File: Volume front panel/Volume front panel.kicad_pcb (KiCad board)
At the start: 2 copper layers, 210.2 x 50.9 mm, 44 parts, among them IC1 MC7805BD2TR4G, IC2 TLC5947DAPR, IC3 MC7805BD2TR4G, J1 26-60-4023, J2 26-60-4023, J3 4328, U1 PEC11R-4330F-S0012, U2 TSOP39238, U3 ISO1541

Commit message: seperated front panel board
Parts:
- moved J2 228.6 mm to (283.5, 78.9), turned to 180 degrees
- moved C13 222.6 mm to (275.0, 79.0), turned to -90 degrees
- moved IC3 214.0 mm to (278.5, 67.0), turned to 0 degrees
- moved C14 205.4 mm to (266.5, 64.0), turned to 180 degrees
- moved C17 202.2 mm to (266.5, 67.0), turned to 180 degrees
- moved C16 199.1 mm to (266.5, 70.0), turned to 180 degrees
- moved J3 189.5 mm to (265.0, 80.0), turned to -90 degrees
- moved R10 186.6 mm to (260.0, 83.0), turned to -90 degrees
- moved R9 183.3 mm to (260.0, 78.0)
- moved U3 170.2 mm to (254.0, 80.0), turned to 0 degrees
- moved C4 14.7 mm to (218.5, 60.5), turned to 180 degrees
- moved J1 13.5 mm to (242.0, 77.1)
- moved C3 12.0 mm to (229.0, 77.0)
- moved C10 11.0 mm to (218.5, 64.0), turned to 180 degrees
- moved IC1 10.5 mm to (230.0, 64.0), turned to 0 degrees
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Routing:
- net Net-(U3-SCL2): track 0.00 -> 7.55 mm
- net Net-(C13-+): track 20.3 -> 27.3 mm
- net Net-(U3-SDA2): track 0.00 -> 6.81 mm
- net GNDI: vias 0 -> 52
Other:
- board size 210.2 x 50.9 mm -> 208 x 50.9 mm

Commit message: moving everything onto front panel, switching psu, no iso
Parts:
- removed the C10 at (218.5, 64.0)
- removed the C11 at (218.5, 67.5)
- removed C13: UUD1V101MNL1GS, Samacsys:CAPAE830X1050N
- removed C14: .1uf, Capacitor_SMD:C_1206_3216Metric
- removed C16: 10uf, Capacitor_SMD:C_1206_3216Metric
- removed C17: 1uf, Capacitor_SMD:C_1206_3216Metric
- removed the C3 at (229.0, 77.0)
- removed the C4 at (218.5, 60.5)
- removed the H1 at (45.0, 50.0)
- removed the H2 at (45.0, 90.0)
- removed the IC1 at (230.0, 64.0)
- removed IC3: MC7805BD2TR4G, Samacsys:TO254P1420X457-4N
- removed J3: 4328, Snapeda_8:ADAFRUIT_4328
- removed R10, R9: 1k, Resistor_SMD:R_1206_3216Metric
- removed the R5 at (190.5, 82.5)
- removed the R6 at (193.0, 82.5)
- removed U3: ISO1541, Package_SO:SOIC-8_3.9x4.9mm_P1.27mm
- added C12: 0.1uf, Capacitor_SMD:C_1206_3216Metric, F.Cu at (159.5, 59.0)
- added C7: UUD1V101MNL1GS, Samacsys:CAPAE830X1050N, F.Cu at (190.0, 55.0)
- added C9: UUD1V101MNL1GS, Samacsys:CAPAE830X1050N, F.Cu at (190.0, 79.0)
- added IC2: TPIC6B595DWR, Samacsys:SOIC127P1030X265-20N, F.Cu at (151.5, 53.0)
- added L1: 150uh, Inductor_SMD:L_Bourns_SRR1260, F.Cu at (190.0, 67.0)
- added PS2: TMPW_5-105, Samacsys:TMPW5112, F.Cu at (202.5, 80.4)
- added R7: 10k, Resistor_SMD:R_1206_3216Metric, F.Cu at (160.5, 49.0)
- J2: value 26-60-4023 -> 10129381-908001BLF; footprint Samacsys:26604023 -> Samacsys:10129381908001BLF
- U1: moved to B.Cu
- moved J2 119.6 mm to (165.8, 57.8), turned to 90 degrees
- moved C1 56.6 mm to (162.0, 85.0), turned to 180 degrees
- moved H2 49.6 mm to (85.5, 87.0)
- moved H1 48.6 mm to (86.5, 47.0)
- moved U1 38.6 mm to (119.0, 74.0), turned to 0 degrees
- moved C3 33.6 mm to (119.5, 56.0)
- moved C4 33.6 mm to (121.9, 71.1)
- moved C5 33.6 mm to (124.5, 56.0)
- moved R1 33.6 mm to (114.5, 59.0)
- moved R2 33.6 mm to (118.5, 62.0)
- moved R3 33.6 mm to (124.5, 62.0)
- moved R4 33.6 mm to (128.5, 59.0)
- moved A1 31.6 mm to (176.6, 63.4)
- moved C2 31.6 mm to (170.5, 82.0)
- moved C10 29.0 mm to (77.1, 62.5)
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- renumbered C12 to C10, C15 to C11, C5 to C3, C6 to C4, C7 to C5, C8 to C6, C9 to C8, H3 to H1, H4 to H2, H5 to H3, H6 to H4, IC2 to IC1, R7 to R5, R8 to R6
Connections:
- A1 pad 10: unconnected-(A1-D7-Pad10) -> unmute
- A1 pad 11: unconnected-(A1-D8-Pad11) -> shift_reg_strobe
- A1 pad 12: unconnected-(A1-D9-Pad12) -> shift_reg_clock
- A1 pad 23: SDA -> unconnected-(A1-A4-Pad23)
- A1 pad 24: SCL -> unconnected-(A1-A5-Pad24)
- A1 pad 5: unconnected-(A1-D2-Pad5) -> Net-(A1-D2)
- A1 pad 9: Net-(A1-D6) -> r_data
- C3 pad 2: Net-(A1-D3) -> Net-(A1-D2)
- C4 pad 1: Net-(A1-D5) -> Net-(A1-D4)
- C5 pad 1: Net-(A1-D4) -> Net-(A1-D3)
- C8 pad 1: Net-(A1-D6) -> Net-(A1-D5)
- J1 pad 2: GNDD -> Net-(PS2-AC_IN_(L))
- J2 pad 1: Net-(C13-+) -> +5V
- J2 pad 2: GNDI -> +5V
- R1 pad 2: Net-(A1-D3) -> Net-(A1-D2)
- R4 pad 2: Net-(A1-D4) -> Net-(A1-D3)
- U1 pad 2: Net-(A1-D5) -> Net-(A1-D4)
- U2 pad 3: Net-(A1-D6) -> Net-(A1-D5)
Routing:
- net +5V-iso: track 44.3 -> 0.00 mm
- net Net-(C13-+): track 27.3 -> 0.00 mm
- net Net-(U3-SCL2): track 7.55 -> 0.00 mm
- net Net-(U3-SDA2): track 6.81 -> 0.00 mm
- net GNDI: vias 52 -> 0
- removed copper zone on B.Cu, net GNDI
- removed copper zone on F.Cu, net GNDI
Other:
- board size 208 x 50.9 mm -> 171 x 50.9 mm

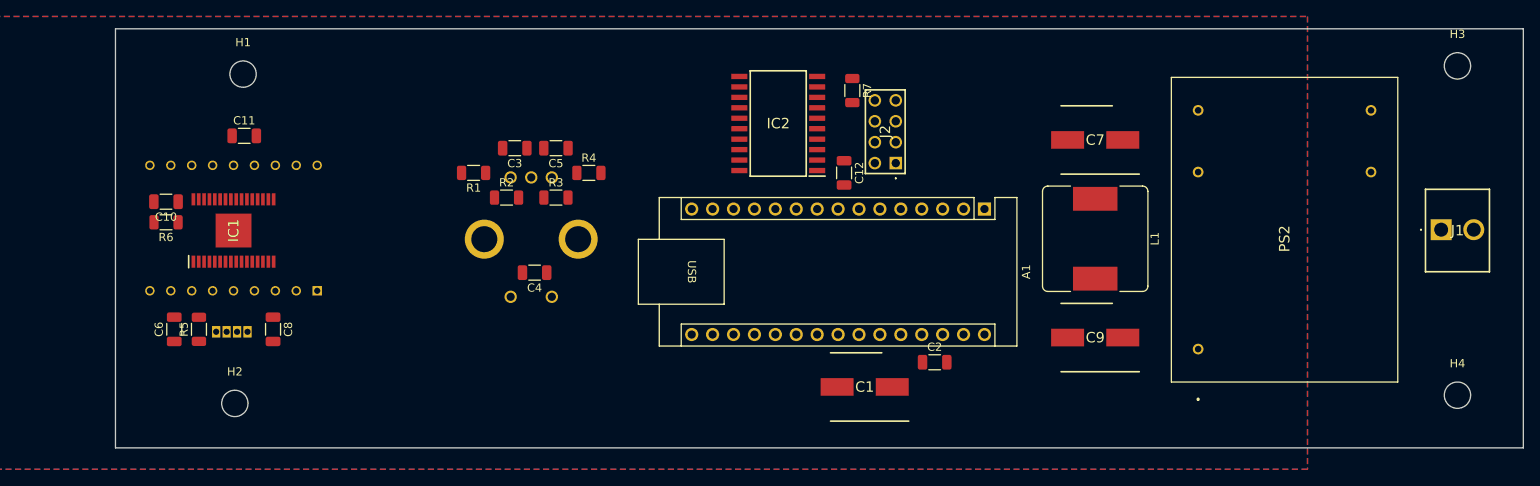
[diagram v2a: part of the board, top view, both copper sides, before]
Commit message: seperate psu, traco. All logic and such on front panel
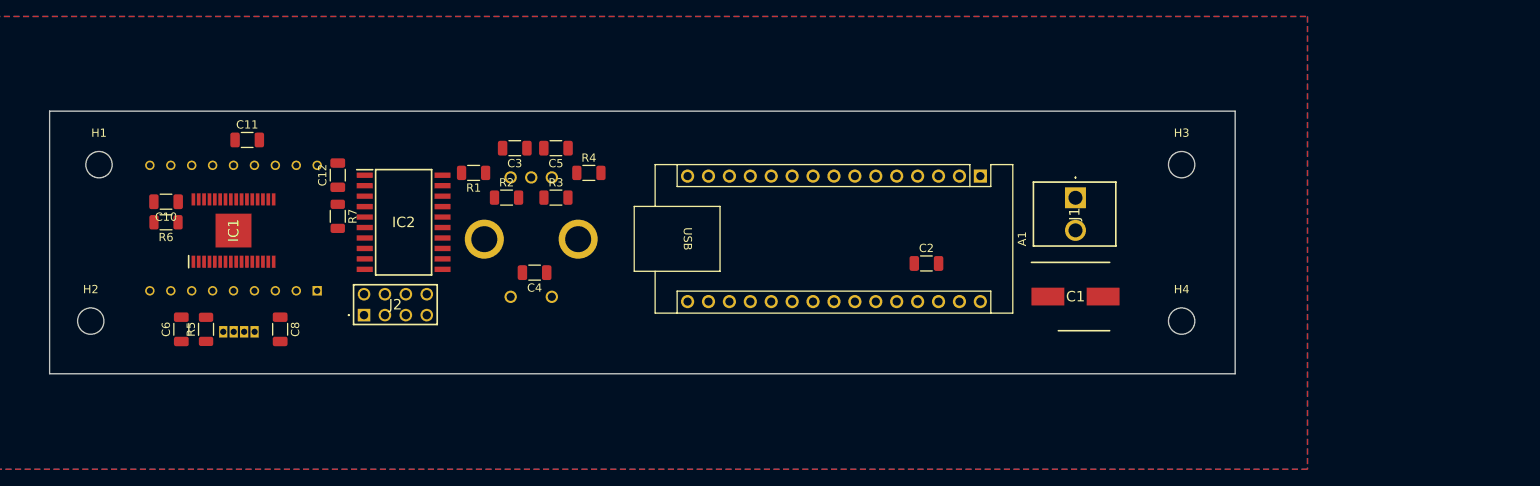
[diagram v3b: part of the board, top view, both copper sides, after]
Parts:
- removed C7, C9: UUD1V101MNL1GS, Samacsys:CAPAE830X1050N
- removed L1: 150uh, Inductor_SMD:L_Bourns_SRR1260
- removed PS2: TMPW_5-105, Samacsys:TMPW5112
- moved J2 67.2 mm to (101.2, 76.3), turned to 0 degrees
- moved R7 64.3 mm to (98.0, 64.3)
- moved C12 61.5 mm to (98.0, 59.3), turned to 90 degrees
- moved IC2 47.1 mm to (106.0, 65.0), turned to 0 degrees
- moved J1 44.6 mm to (187.6, 62.0), turned to 90 degrees
- moved H3 35.6 mm to (200.5, 58.0)
- moved H4 34.7 mm to (200.5, 77.0)
- moved C1 27.9 mm to (187.6, 74.0), turned to 0 degrees
- moved H1 20.7 mm to (69.0, 58.0)
- moved H2 20.2 mm to (68.0, 77.0)
- moved C2 12.0 mm to (169.5, 70.0)
- moved A1 4.03 mm to (176.1, 59.4)
- moved C6 0.86 mm to (79.0, 78.0)
- moved C8 0.86 mm to (91.0, 78.0)
- moved R5 0.86 mm to (82.0, 78.0)
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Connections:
- J1 pad 1: Net-(PS2-AC_IN_(N)) -> +5V
- J1 pad 2: Net-(PS2-AC_IN_(L)) -> GNDD
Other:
- board size 171 x 50.9 mm -> 144 x 31.9 mm

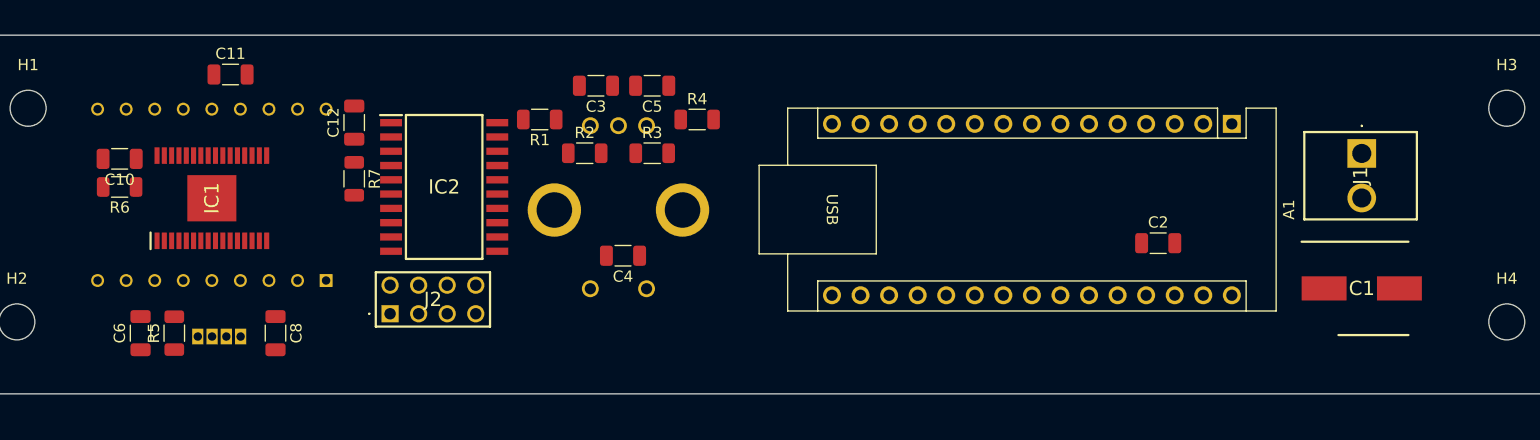
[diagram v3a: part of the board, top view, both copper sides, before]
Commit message: audio board, using rlxpassive base
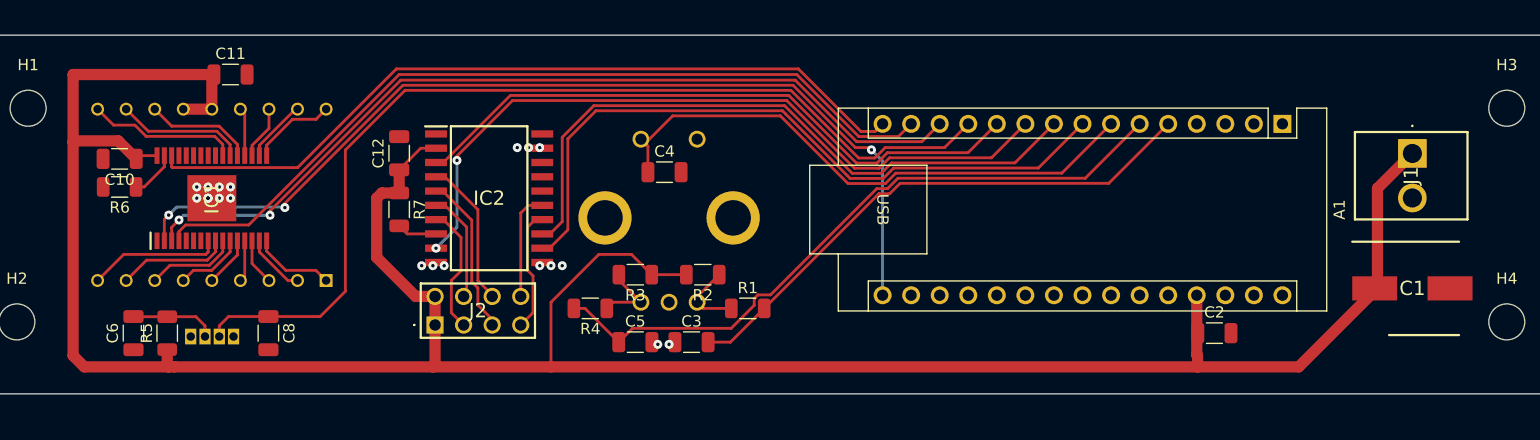
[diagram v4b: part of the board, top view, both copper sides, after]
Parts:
- moved R1 25.0 mm to (133.0, 75.8), turned to 0 degrees
- moved C3 24.3 mm to (128.0, 78.8), turned to 0 degrees
- moved C5 22.8 mm to (123.0, 78.8), turned to 0 degrees
- moved R4 19.3 mm to (119.0, 75.8), turned to 180 degrees
- moved U1 16.3 mm to (128.5, 60.8), turned to 180 degrees
- moved R2 15.1 mm to (129.0, 72.8), turned to 180 degrees
- moved R3 10.9 mm to (123.0, 72.8), turned to 180 degrees
- moved C2 9.43 mm to (174.5, 78.0)
- moved C4 8.30 mm to (125.6, 63.7), turned to 0 degrees
- moved C12 4.84 mm to (102.0, 62.0)
- moved R7 4.84 mm to (102.0, 67.0)
- moved A1 4.50 mm to (180.6, 59.4)
- moved C1 4.50 mm to (192.1, 74.0)
- moved J1 4.50 mm to (192.1, 62.0)
- moved IC2 4.12 mm to (110.0, 66.0)
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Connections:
- A1 pad 11: shift_reg_strobe -> r_data
- A1 pad 12: shift_reg_clock -> Net-(A1-D9)
- A1 pad 13: data -> sclk
- A1 pad 14: sclk -> data
- A1 pad 8: Net-(A1-D5) -> shift_reg_clock
- A1 pad 9: r_data -> shift_reg_strobe
- C8 pad 1: Net-(A1-D5) -> Net-(A1-D9)
- IC2 pad 14: r5 -> r4
- IC2 pad 15: r4 -> r5
- J2 pad 4: r0 -> r2
- J2 pad 5: r4 -> r1
- J2 pad 6: r1 -> r0
- J2 pad 7: r5 -> r4
- J2 pad 8: r2 -> r5
- U2 pad 3: Net-(A1-D5) -> Net-(A1-D9)
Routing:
- net +5V: track 0.00 -> 238.9 mm
- net Net-(A1-D9): track 0.00 -> 86.7 mm
- net blank: track 0.00 -> 85.9 mm, vias 0 -> 3
- net sclk: track 0.00 -> 78.1 mm, vias 0 -> 2
- net data: track 0.00 -> 74.5 mm
- net xlat: track 0.00 -> 70.5 mm
- net unmute: track 0.00 -> 65.7 mm, vias 0 -> 2
- net shift_reg_clock: track 0.00 -> 62.4 mm
- net Net-(A1-D3): track 0.00 -> 59.9 mm
- net shift_reg_strobe: track 0.00 -> 58.9 mm
- net r_data: track 0.00 -> 56.3 mm
- net Net-(A1-D4): track 0.00 -> 50.5 mm
- net Net-(A1-D2): track 0.00 -> 49.0 mm
- net r1: track 0.00 -> 14.3 mm
- net Net-(DS1-SEGMENT_"B2"): track 0.00 -> 13.4 mm
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
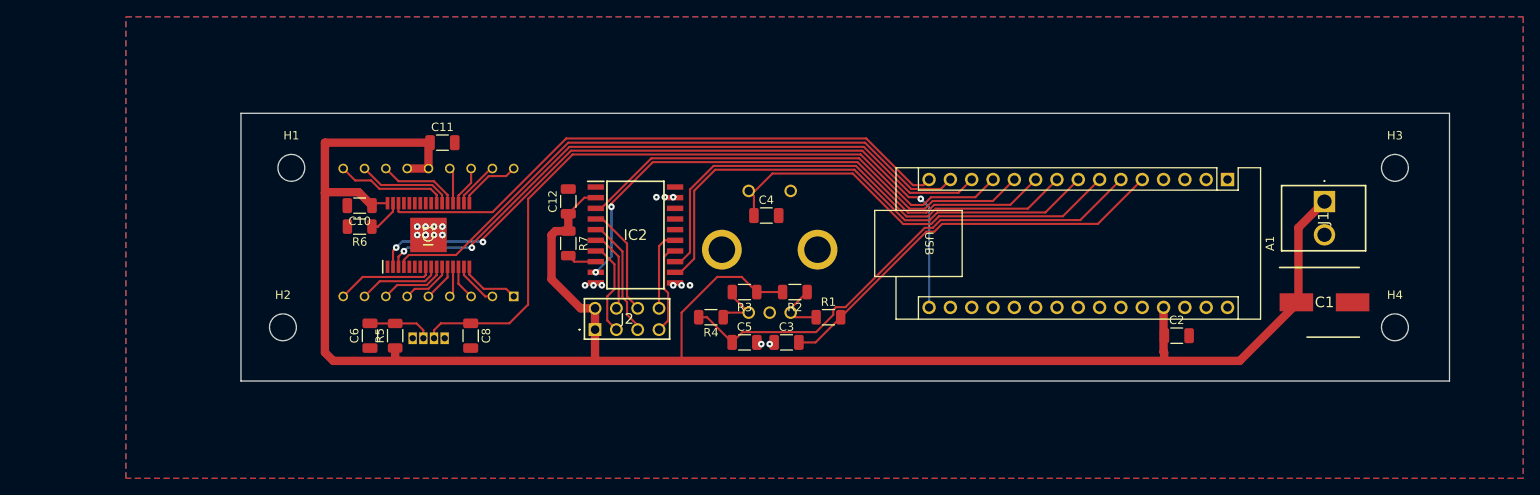
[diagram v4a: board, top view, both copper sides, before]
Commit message: Switch panel seperate, going to integrate i2c onto volume now
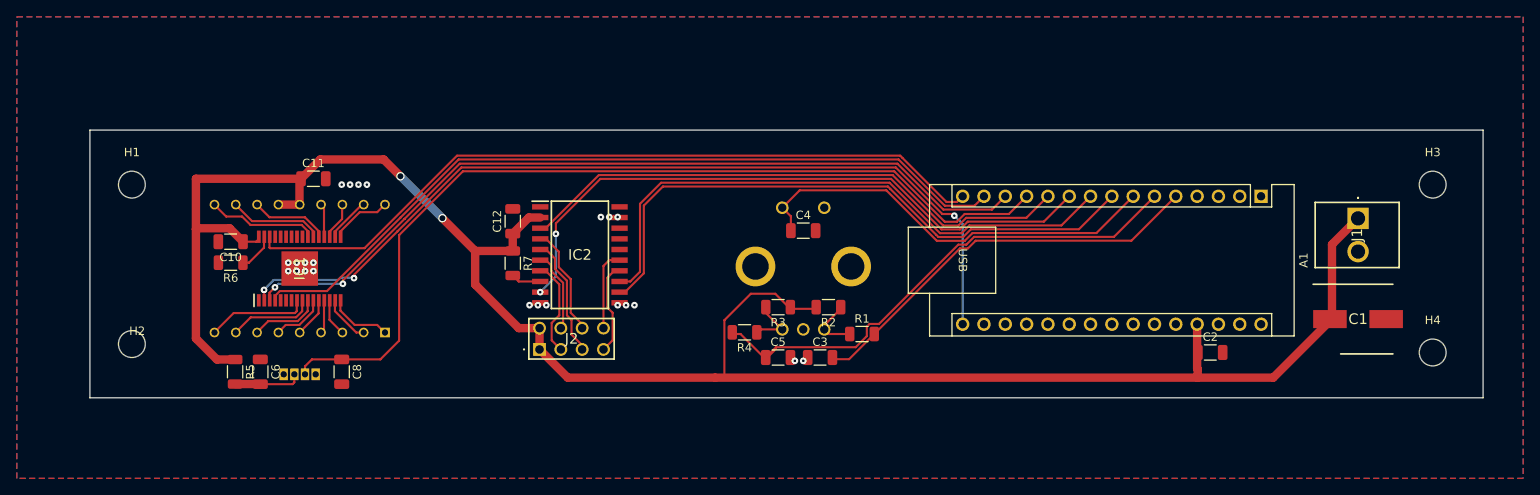
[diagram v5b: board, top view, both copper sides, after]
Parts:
- moved DS1 25.7 mm to (70.0, 70.0)
- moved R5 19.5 mm to (62.3, 82.3), turned to -90 degrees
- moved H1 19.1 mm to (50.0, 60.0)
- moved H2 18.1 mm to (50.0, 79.0)
- moved C11 16.0 mm to (71.6, 59.3)
- moved C8 16.0 mm to (75.0, 82.3)
- moved U2 16.0 mm to (70.0, 82.3)
- moved C10 16.0 mm to (61.8, 66.8)
- moved R6 16.0 mm to (61.8, 69.3)
- moved IC1 15.9 mm to (70.0, 70.0)
- moved C6 13.8 mm to (65.3, 82.3), turned to -90 degrees
- moved U1 9.37 mm to (130.0, 70.0)
- moved C12 7.03 mm to (95.4, 64.4)
- moved IC2 7.03 mm to (103.4, 68.4)
- moved J2 7.03 mm to (98.6, 79.6)
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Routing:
- net data: track 74.5 -> 94.9 mm
- net sclk: track 78.1 -> 98.4 mm
- net Net-(A1-D9): track 86.7 -> 107.0 mm
- net blank: track 85.9 -> 106.2 mm
- net xlat: track 70.5 -> 90.7 mm
- net shift_reg_strobe: track 58.9 -> 70.1 mm
- net unmute: track 65.7 -> 76.5 mm
- net r_data: track 56.3 -> 67.1 mm
- net shift_reg_clock: track 62.4 -> 73.1 mm
- net +5V: track 238.9 -> 244.1 mm, vias 0 -> 2
- net Net-(A1-D3): track 59.9 -> 61.9 mm
- net Net-(A1-D4): track 50.5 -> 51.1 mm
- net GNDD: vias 20 -> 24
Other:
- board size 144 x 31.9 mm -> 166 x 31.9 mm

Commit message: likely all done with v1, mainboard obsolete
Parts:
- removed the C12 at (95.4, 64.4)
- removed the C4 at (130.0, 65.5)
- removed H1, H2, H3, H4: MountingHole, MountingHole:MountingHole_3.2mm_M3_ISO7380
- removed IC2: TPIC6B595DWR, Samacsys:SOIC127P1030X265-20N
- removed the R7 at (95.4, 69.4)
- added C2: 0.01uf, Capacitor_SMD:C_1206_3216Metric, F.Cu at (78.0, 105.0)
- added C3: 0.01uf, Capacitor_SMD:C_1206_3216Metric, F.Cu at (70.0, 90.0)
- added C5: 0.01uf, Capacitor_SMD:C_1206_3216Metric, F.Cu at (63.0, 105.0)
- added C7: 0.01uf, Capacitor_SMD:C_1206_3216Metric, F.Cu at (230.1, 89.4)
- added R1: 10k, Resistor_SMD:R_1206_3216Metric, F.Cu at (78.0, 108.0)
- added R11: 4.7k, Resistor_SMD:R_1206_3216Metric, F.Cu at (106.0, 100.0)
- added R12: 10k, Resistor_SMD:R_1206_3216Metric, F.Cu at (141.8, 101.8)
- added R2: 10k, Resistor_SMD:R_1206_3216Metric, F.Cu at (73.0, 111.0)
- added R3: 10k, Resistor_SMD:R_1206_3216Metric, F.Cu at (67.0, 111.0)
- added R4: 10k, Resistor_SMD:R_1206_3216Metric, F.Cu at (63.0, 108.0)
- added R9: 4.7k, Resistor_SMD:R_1206_3216Metric, F.Cu at (106.0, 96.7)
- added U1: PEC11R-4330F-S0012, Samacsys:PEC11R4330FS0012, B.Cu at (70.0, 100.0)
- J1: value 26-60-4023 -> BHR-06-VUA; footprint Samacsys:26604023 -> Samacsys:SHDR6W64P254_2X3_1522X880X920P
- J2: value 10129381-908001BLF -> BHR-06-VUA; footprint Samacsys:10129381908001BLF -> Samacsys:SHDR6W64P254_2X3_1522X880X920P
- moved C6 107.7 mm to (237.1, 104.4)
- moved R6 106.3 mm to (233.1, 110.4)
- moved R7 106.3 mm to (227.1, 110.4)
- moved R5 104.4 mm to (237.0, 107.8)
- moved R8 104.4 mm to (223.0, 107.6)
- moved U2 104.4 mm to (230.0, 100.0)
- moved C8 99.0 mm to (223.1, 104.4)
- moved C12 85.7 mm to (151.6, 90.0)
- moved C9 85.4 mm to (145.3, 112.3)
- moved R10 85.4 mm to (142.3, 112.3)
- moved C10 85.4 mm to (155.0, 112.3)
- moved C11 85.4 mm to (141.8, 96.8)
- moved DS1 85.4 mm to (150.0, 100.0)
- moved IC1 85.4 mm to (150.0, 100.0)
- moved R13 85.4 mm to (141.8, 99.3)
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- renumbered C8 to C10, C10 to C11, C11 to C12, C2 to C4, C3 to C6, C5 to C8, C6 to C9, R5 to R10, R6 to R13, R1 to R5, R2 to R6, R3 to R7, R4 to R8, U1 to U2, U2 to U3
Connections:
- A1 pad 10: unmute -> Net-(A1-D7)
- A1 pad 11: r_data -> IR
- A1 pad 12: Net-(A1-D9) -> unconnected-(A1-D9-Pad12)
- A1 pad 13: sclk -> unconnected-(A1-D10-Pad13)
- A1 pad 14: data -> unconnected-(A1-D11-Pad14)
- A1 pad 15: xlat -> unconnected-(A1-D12-Pad15)
- A1 pad 16: blank -> unconnected-(A1-D13-Pad16)
- A1 pad 19: unconnected-(A1-A0-Pad19) -> data
- A1 pad 20: unconnected-(A1-A1-Pad20) -> sclk
- A1 pad 21: unconnected-(A1-A2-Pad21) -> blank
- A1 pad 22: unconnected-(A1-A3-Pad22) -> xlat
- A1 pad 23: unconnected-(A1-A4-Pad23) -> SDA
- A1 pad 24: unconnected-(A1-A5-Pad24) -> SCL
- A1 pad 8: shift_reg_clock -> Net-(A1-D5)
- A1 pad 9: shift_reg_strobe -> Net-(A1-D6)
- C10 pad 1: Net-(A1-D9) -> IR
- C8 pad 1: Net-(A1-D3) -> Net-(A1-D5)
- J2 pad 3: r3 -> GNDD
- J2 pad 4: r2 -> GNDD
- J2 pad 5: r1 -> SCL
- J2 pad 6: r0 -> SDA
- R8 pad 2: Net-(A1-D3) -> Net-(A1-D5)
- U2 pad 2: Net-(A1-D4) -> Net-(A1-D7)
- U3 pad 3: Net-(A1-D9) -> IR
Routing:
- net Net-(A1-D6): track 0.00 -> 135.3 mm, vias 0 -> 1
- net SCL: track 0.00 -> 126.4 mm, vias 0 -> 1
- net SDA: track 0.00 -> 119.3 mm, vias 0 -> 1
- net Net-(A1-D9): track 107.0 -> 0.00 mm
- net Net-(A1-D4): track 51.1 -> 152.2 mm, vias 0 -> 1
- net Net-(A1-D3): track 61.9 -> 144.4 mm
- net unmute: track 76.5 -> 0.00 mm, vias 2 -> 0
- net shift_reg_clock: track 73.1 -> 0.00 mm
- net shift_reg_strobe: track 70.1 -> 0.00 mm
- net r_data: track 67.1 -> 0.00 mm
- net IR: track 0.00 -> 52.7 mm, vias 0 -> 4
- net blank: track 106.2 -> 54.5 mm, vias 3 -> 2
- net data: track 94.9 -> 43.3 mm
- net sclk: track 98.4 -> 47.7 mm
- net +5V: track 244.1 -> 294.6 mm, vias 2 -> 0
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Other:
- board size 166 x 31.9 mm -> 199 x 31.9 mm
